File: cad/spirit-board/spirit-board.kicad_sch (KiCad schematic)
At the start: 0 parts

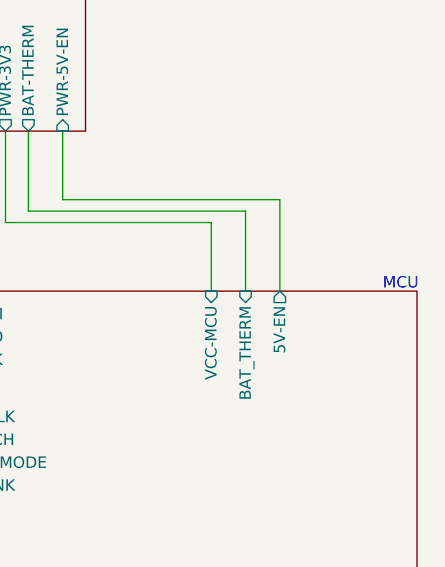
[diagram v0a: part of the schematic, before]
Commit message: per-coil schematic
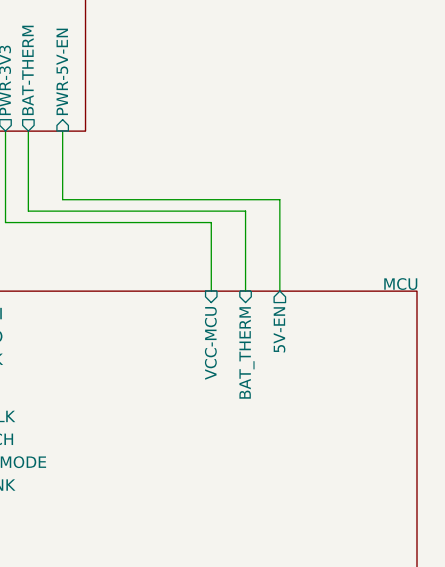
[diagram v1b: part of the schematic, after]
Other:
- note removed: "MCU"
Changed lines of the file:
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@@
     (stroke (width 0) (type default))
-  )
-  (text "MCU" (at 168.91 68.58 0)
-    (effects (font (size 1.27 1.27)) (justify left bottom))
   )
   (sheet (at 92.71 21.59) (size 43.18 29.21)
@@
     )
   )
-  (sheet (at 120.65 68.58) (size 52.07 36.83) (fields_autoplaced)
+  (sheet (at 120.65 68.58) (size 52.07 36.83)
     (stroke (width 0.1524) (type solid))
     (fill (color 0 0 0 0.0000))
-    (property "Sheetname" "MCU" (at 120.65 67.8684 0)
-      (effects (font (size 1.27 1.27)) (justify left bottom) hide)
+    (property "Sheetname" "MCU" (at 168.91 68.58 0)
+      (effects (font (size 1.27 1.27)) (justify left bottom))
     )
     (property "Sheetfile" "mcu.kicad_sch" (at 120.65 105.9946 0)
